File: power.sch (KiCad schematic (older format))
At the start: 13 parts, among them P1 POWER, Q2 DMP3056L-7, U1 REG1117-3.3, U2 REG1117A-2.5, U3 REG1117A-1.8

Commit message: Assigned footprints to most components
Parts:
- removed C9: 1uF, symbol CP1
- added C9: 1uF, Capacitors_SMD:C_0805, symbol C
- C10, C11, C12, C13, C14, C15: footprint (none) -> Capacitors_Tantalum_SMD:CP_Tantalum_Case-C_EIA-6032-28_Reflow
- F1: footprint (none) -> Fuse_Holders_and_Fuses:Fuse_CB61F
- P1: footprint (none) -> Connectors:USB_Micro-B
- Q2: footprint (none) -> TO_SOT_Packages_SMD:SOT-23
- U1, U2, U3: footprint SOT-223 -> TO_SOT_Packages_SMD:SOT-223-3_TabPin2
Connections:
- net +5V: now also C9.1
- net GND: now also C9.2
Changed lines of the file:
@@
 F 0 "U1" H 4000 1750 50  0000 C CNN
 F 1 "REG1117-3.3" H 4000 1700 50  0000 C CNN
-F 2 "SOT-223" H 4000 1600 50  0000 C CNN
+F 2 "TO_SOT_Packages_SMD:SOT-223-3_TabPin2" H 4000 1600 50  0000 C CNN
 F 3 "" H 4000 1500 50  0000 C CNN
 	1    4000 1500
@@
 F 0 "U2" H 6100 1750 50  0000 C CNN
 F 1 "REG1117A-2.5" H 6100 1700 50  0000 C CNN
-F 2 "SOT-223" H 6100 1600 50  0000 C CNN
+F 2 "TO_SOT_Packages_SMD:SOT-223-3_TabPin2" H 6100 1600 50  0000 C CNN
 F 3 "" H 6100 1500 50  0000 C CNN
 	1    6100 1500
@@
 F 0 "U3" H 8100 1750 50  0000 C CNN
 F 1 "REG1117A-1.8" H 8100 1700 50  0000 C CNN
-F 2 "SOT-223" H 8100 1600 50  0000 C CNN
+F 2 "TO_SOT_Packages_SMD:SOT-223-3_TabPin2" H 8100 1600 50  0000 C CNN
 F 3 "" H 8100 1500 50  0000 C CNN
 	1    8100 1500
@@
 F 0 "C10" H 3325 1900 50  0000 L CNN
 F 1 "10uF" H 3325 1700 50  0000 L CNN
-F 2 "" H 3300 1800 50  0000 C CNN
+F 2 "Capacitors_Tantalum_SMD:CP_Tantalum_Case-C_EIA-6032-28_Reflow" H 3300 1800 50  0001 C CNN
 F 3 "" H 3300 1800 50  0000 C CNN
 	1    3300 1800
@@
 F 0 "C12" H 5425 1900 50  0000 L CNN
 F 1 "10uF" H 5425 1700 50  0000 L CNN
-F 2 "" H 5400 1800 50  0000 C CNN
+F 2 "Capacitors_Tantalum_SMD:CP_Tantalum_Case-C_EIA-6032-28_Reflow" H 5400 1800 50  0001 C CNN
 F 3 "" H 5400 1800 50  0000 C CNN
 	1    5400 1800
@@
 F 0 "C11" H 4725 1900 50  0000 L CNN
 F 1 "10uF" H 4725 1700 50  0000 L CNN
-F 2 "" H 4700 1800 50  0000 C CNN
+F 2 "Capacitors_Tantalum_SMD:CP_Tantalum_Case-C_EIA-6032-28_Reflow" H 4700 1800 50  0001 C CNN
 F 3 "" H 4700 1800 50  0000 C CNN
 	1    4700 1800
@@
 F 0 "C13" H 6825 1900 50  0000 L CNN
 F 1 "10uF" H 6825 1700 50  0000 L CNN
-F 2 "" H 6800 1800 50  0000 C CNN
+F 2 "Capacitors_Tantalum_SMD:CP_Tantalum_Case-C_EIA-6032-28_Reflow" H 6800 1800 50  0001 C CNN
 F 3 "" H 6800 1800 50  0000 C CNN
 	1    6800 1800
@@
 F 0 "C14" H 7425 1900 50  0000 L CNN
 F 1 "10uF" H 7425 1700 50  0000 L CNN
-F 2 "" H 7400 1800 50  0000 C CNN
+F 2 "Capacitors_Tantalum_SMD:CP_Tantalum_Case-C_EIA-6032-28_Reflow" H 7400 1800 50  0001 C CNN
 F 3 "" H 7400 1800 50  0000 C CNN
 	1    7400 1800
@@
 F 0 "C15" H 8825 1900 50  0000 L CNN
 F 1 "10uF" H 8825 1700 50  0000 L CNN
-F 2 "" H 8800 1800 50  0000 C CNN
+F 2 "Capacitors_Tantalum_SMD:CP_Tantalum_Case-C_EIA-6032-28_Reflow" H 8800 1800 50  0001 C CNN
 F 3 "" H 8800 1800 50  0000 C CNN
 	1    8800 1800
@@
 F 0 "P1" H 1475 1425 50  0000 C CNN
 F 1 "POWER" H 1150 1750 50  0000 C CNN
-F 2 "" V 1100 1450 50  0000 C CNN
+F 2 "Connectors:USB_Micro-B" V 1100 1450 50  0001 C CNN
 F 3 "" V 1100 1450 50  0000 C CNN
 	1    1150 1550
@@
 F 0 "F1" V 1780 1350 50  0000 C CNN
 F 1 "2.5A" V 1625 1350 50  0000 C CNN
-F 2 "" V 1630 1350 50  0000 C CNN
+F 2 "Fuse_Holders_and_Fuses:Fuse_CB61F" V 1630 1350 50  0001 C CNN
 F 3 "" H 1700 1350 50  0000 C CNN
 	1    1700 1350
 	0    1    1    0
-$EndComp
-$Comp
-L CP1 C9
-U 1 1 5C122ABE
-P 2600 1800
-F 0 "C9" H 2625 1900 50  0000 L CNN
-F 1 "1uF" H 2625 1700 50  0000 L CNN
-F 2 "" H 2600 1800 50  0000 C CNN
-F 3 "" H 2600 1800 50  0000 C CNN
-	1    2600 1800
-	1    0    0    -1
 $EndComp
 $Comp
@@
 F 0 "Q2" H 2350 1500 50  0000 L CNN
 F 1 "DMP3056L-7" H 2350 1400 50  0000 L CNN
-F 2 "" H 2350 1550 50  0000 C CNN
+F 2 "TO_SOT_Packages_SMD:SOT-23" H 2350 1550 50  0001 C CNN
 F 3 "" H 2150 1450 50  0000 C CNN
 	1    2150 1450
@@
 Wire Wire Line
 	9450 2100 9450 1000
+$Comp
+L C C9
+U 1 1 5C14646A
+P 2600 1800
+F 0 "C9" H 2625 1900 50  0000 L CNN
+F 1 "1uF" H 2625 1700 50  0000 L CNN
+F 2 "Capacitors_SMD:C_0805" H 2638 1650 50  0001 C CNN
+F 3 "" H 2600 1800 50  0000 C CNN
+	1    2600 1800
+	1    0    0    -1
+$EndComp
 $EndSCHEMATC

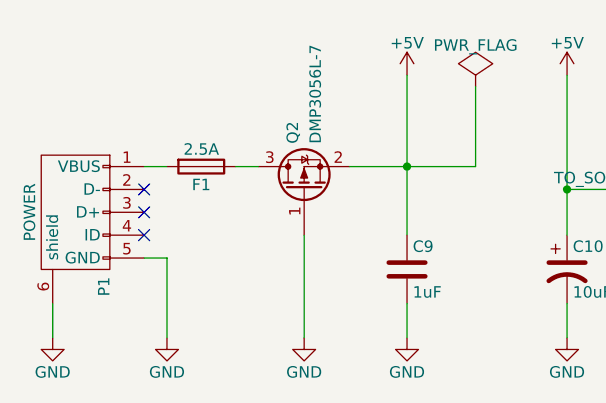
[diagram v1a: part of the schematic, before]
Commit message: Fixed fused
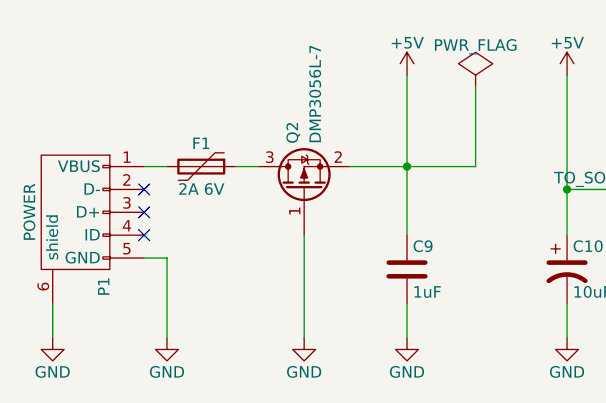
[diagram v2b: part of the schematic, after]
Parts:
- removed F1: 2.5A, Fuse_Holders_and_Fuses:Fuse_CB61F, symbol Fuse
- added F1: 2A 6V, Polyfuse_Bourns_MF-PSML:Polyfuse_0805, symbol Polyfuse
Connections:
- net at P1.1 (VBUS): now also F1.2
- net at Q2.3 (D): now also F1.1
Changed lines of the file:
@@
-$EndComp
-$Comp
-L Fuse F1
-U 1 1 5C1225FC
-P 1700 1350
-F 0 "F1" V 1780 1350 50  0000 C CNN
-F 1 "2.5A" V 1625 1350 50  0000 C CNN
-F 2 "Fuse_Holders_and_Fuses:Fuse_CB61F" V 1630 1350 50  0001 C CNN
-F 3 "" H 1700 1350 50  0000 C CNN
-	1    1700 1350
-	0    1    1    0
 $EndComp
 $Comp
@@
 	1    0    0    -1
 $EndComp
+$Comp
+L Polyfuse F1
+U 1 1 5C16EB7F
+P 1700 1350
+F 0 "F1" V 1600 1350 50  0000 C CNN
+F 1 "2A 6V" V 1800 1350 50  0000 C CNN
+F 2 "Polyfuse_Bourns_MF-PSML:Polyfuse_0805" H 1750 1150 50  0001 L CNN
+F 3 "" H 1700 1350 50  0001 C CNN
+	1    1700 1350
+	0    1    1    0
+$EndComp
 $EndSCHEMATC

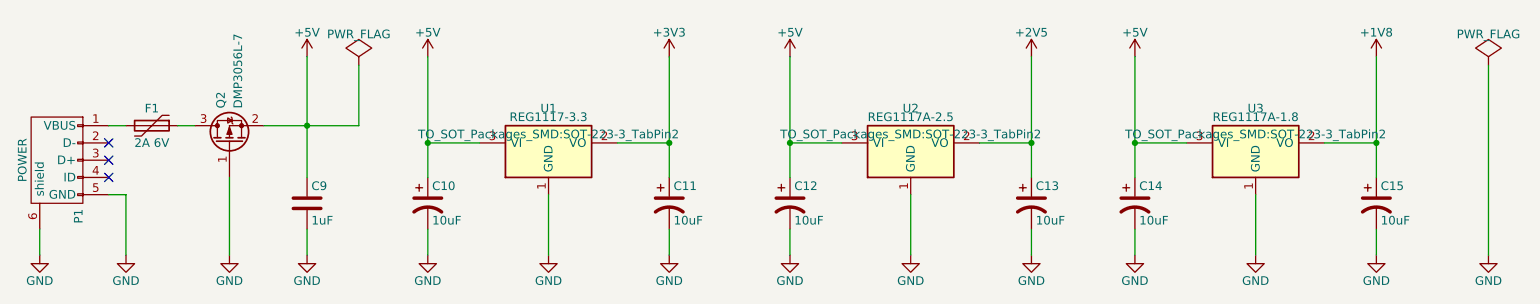
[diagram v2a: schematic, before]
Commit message: Removed 2.5V regulator and changed bottom ground plane clearence
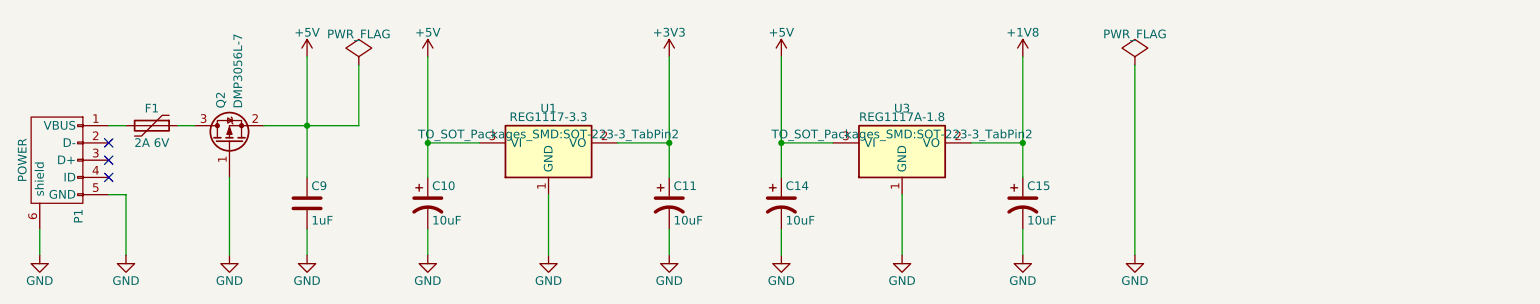
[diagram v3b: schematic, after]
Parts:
- removed C12, C13: 10uF, Capacitors_Tantalum_SMD:CP_Tantalum_Case-C_EIA-6032-28_Reflow, symbol CP1
- removed U2: REG1117A-2.5, TO_SOT_Packages_SMD:SOT-223-3_TabPin2, symbol REG1117A-2.5
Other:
- moved on the sheet: C14, C15, U3
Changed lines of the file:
@@
-$EndComp
-$Comp
-L REG1117A-2.5 U2
-U 1 1 5C11A1F2
-P 6100 1500
-F 0 "U2" H 6100 1750 50  0000 C CNN
-F 1 "REG1117A-2.5" H 6100 1700 50  0000 C CNN
-F 2 "TO_SOT_Packages_SMD:SOT-223-3_TabPin2" H 6100 1600 50  0000 C CNN
-F 3 "" H 6100 1500 50  0000 C CNN
-	1    6100 1500
-	1    0    0    -1
 $EndComp
 $Comp
 L REG1117A-1.8 U3
 U 1 1 5C11A22F
-P 8100 1500
-F 0 "U3" H 8100 1750 50  0000 C CNN
-F 1 "REG1117A-1.8" H 8100 1700 50  0000 C CNN
-F 2 "TO_SOT_Packages_SMD:SOT-223-3_TabPin2" H 8100 1600 50  0000 C CNN
-F 3 "" H 8100 1500 50  0000 C CNN
-	1    8100 1500
+P 6050 1500
+F 0 "U3" H 6050 1750 50  0000 C CNN
+F 1 "REG1117A-1.8" H 6050 1700 50  0000 C CNN
+F 2 "TO_SOT_Packages_SMD:SOT-223-3_TabPin2" H 6050 1600 50  0000 C CNN
+F 3 "" H 6050 1500 50  0000 C CNN
+	1    6050 1500
 	1    0    0    -1
 $EndComp
@@
 $EndComp
 $Comp
-L +5V #PWR031
-U 1 1 5C11A6C8
-P 5400 950
-F 0 "#PWR031" H 5400 800 50  0001 C CNN
-F 1 "+5V" H 5400 1090 50  0000 C CNN
-F 2 "" H 5400 950 50  0000 C CNN
-F 3 "" H 5400 950 50  0000 C CNN
-	1    5400 950
-	1    0    0    -1
-$EndComp
-$Comp
-L CP1 C12
-U 1 1 5C11A6CF
-P 5400 1800
-F 0 "C12" H 5425 1900 50  0000 L CNN
-F 1 "10uF" H 5425 1700 50  0000 L CNN
-F 2 "Capacitors_Tantalum_SMD:CP_Tantalum_Case-C_EIA-6032-28_Reflow" H 5400 1800 50  0001 C CNN
-F 3 "" H 5400 1800 50  0000 C CNN
-	1    5400 1800
-	1    0    0    -1
-$EndComp
-$Comp
-L GND #PWR032
-U 1 1 5C11A6D7
-P 5400 2100
-F 0 "#PWR032" H 5400 1850 50  0001 C CNN
-F 1 "GND" H 5400 1950 50  0000 C CNN
-F 2 "" H 5400 2100 50  0000 C CNN
-F 3 "" H 5400 2100 50  0000 C CNN
-	1    5400 2100
-	1    0    0    -1
-$EndComp
-$Comp
-L GND #PWR033
-U 1 1 5C11A6DD
-P 6100 2100
-F 0 "#PWR033" H 6100 1850 50  0001 C CNN
-F 1 "GND" H 6100 1950 50  0000 C CNN
-F 2 "" H 6100 2100 50  0000 C CNN
-F 3 "" H 6100 2100 50  0000 C CNN
-	1    6100 2100
-	1    0    0    -1
-$EndComp
-$Comp
 L CP1 C11
 U 1 1 5C11A780
@@
 $EndComp
 $Comp
-L CP1 C13
-U 1 1 5C11A7E8
-P 6800 1800
-F 0 "C13" H 6825 1900 50  0000 L CNN
-F 1 "10uF" H 6825 1700 50  0000 L CNN
-F 2 "Capacitors_Tantalum_SMD:CP_Tantalum_Case-C_EIA-6032-28_Reflow" H 6800 1800 50  0001 C CNN
-F 3 "" H 6800 1800 50  0000 C CNN
-	1    6800 1800
-	1    0    0    -1
-$EndComp
-$Comp
-L GND #PWR035
-U 1 1 5C11A7EF
-P 6800 2100
-F 0 "#PWR035" H 6800 1850 50  0001 C CNN
-F 1 "GND" H 6800 1950 50  0000 C CNN
-F 2 "" H 6800 2100 50  0000 C CNN
-F 3 "" H 6800 2100 50  0000 C CNN
-	1    6800 2100
-	1    0    0    -1
-$EndComp
-$Comp
 L +5V #PWR036
 U 1 1 5C11A92B
-P 7400 950
-F 0 "#PWR036" H 7400 800 50  0001 C CNN
-F 1 "+5V" H 7400 1090 50  0000 C CNN
-F 2 "" H 7400 950 50  0000 C CNN
-F 3 "" H 7400 950 50  0000 C CNN
-	1    7400 950
+P 5350 950
+F 0 "#PWR036" H 5350 800 50  0001 C CNN
+F 1 "+5V" H 5350 1090 50  0000 C CNN
+F 2 "" H 5350 950 50  0000 C CNN
+F 3 "" H 5350 950 50  0000 C CNN
+	1    5350 950
 	1    0    0    -1
 $EndComp
@@
 L CP1 C14
 U 1 1 5C11A932
-P 7400 1800
-F 0 "C14" H 7425 1900 50  0000 L CNN
-F 1 "10uF" H 7425 1700 50  0000 L CNN
-F 2 "Capacitors_Tantalum_SMD:CP_Tantalum_Case-C_EIA-6032-28_Reflow" H 7400 1800 50  0001 C CNN
-F 3 "" H 7400 1800 50  0000 C CNN
-	1    7400 1800
+P 5350 1800
+F 0 "C14" H 5375 1900 50  0000 L CNN
+F 1 "10uF" H 5375 1700 50  0000 L CNN
+F 2 "Capacitors_Tantalum_SMD:CP_Tantalum_Case-C_EIA-6032-28_Reflow" H 5350 1800 50  0001 C CNN
+F 3 "" H 5350 1800 50  0000 C CNN
+	1    5350 1800
 	1    0    0    -1
 $EndComp
@@
 L GND #PWR037
 U 1 1 5C11A93A
-P 7400 2100
-F 0 "#PWR037" H 7400 1850 50  0001 C CNN
-F 1 "GND" H 7400 1950 50  0000 C CNN
-F 2 "" H 7400 2100 50  0000 C CNN
-F 3 "" H 7400 2100 50  0000 C CNN
-	1    7400 2100
+P 5350 2100
+F 0 "#PWR037" H 5350 1850 50  0001 C CNN
+F 1 "GND" H 5350 1950 50  0000 C CNN
+F 2 "" H 5350 2100 50  0000 C CNN
+F 3 "" H 5350 2100 50  0000 C CNN
+	1    5350 2100
 	1    0    0    -1
 $EndComp
@@
 L GND #PWR038
 U 1 1 5C11A940
-P 8100 2100
-F 0 "#PWR038" H 8100 1850 50  0001 C CNN
-F 1 "GND" H 8100 1950 50  0000 C CNN
-F 2 "" H 8100 2100 50  0000 C CNN
-F 3 "" H 8100 2100 50  0000 C CNN
-	1    8100 2100
+P 6050 2100
+F 0 "#PWR038" H 6050 1850 50  0001 C CNN
+F 1 "GND" H 6050 1950 50  0000 C CNN
+F 2 "" H 6050 2100 50  0000 C CNN
+F 3 "" H 6050 2100 50  0000 C CNN
+	1    6050 2100
 	1    0    0    -1
 $EndComp
@@
 L CP1 C15
 U 1 1 5C11A94D
-P 8800 1800
-F 0 "C15" H 8825 1900 50  0000 L CNN
-F 1 "10uF" H 8825 1700 50  0000 L CNN
-F 2 "Capacitors_Tantalum_SMD:CP_Tantalum_Case-C_EIA-6032-28_Reflow" H 8800 1800 50  0001 C CNN
-F 3 "" H 8800 1800 50  0000 C CNN
-	1    8800 1800
+P 6750 1800
+F 0 "C15" H 6775 1900 50  0000 L CNN
+F 1 "10uF" H 6775 1700 50  0000 L CNN
+F 2 "Capacitors_Tantalum_SMD:CP_Tantalum_Case-C_EIA-6032-28_Reflow" H 6750 1800 50  0001 C CNN
+F 3 "" H 6750 1800 50  0000 C CNN
+	1    6750 1800
 	1    0    0    -1
 $EndComp
@@
 L GND #PWR039
 U 1 1 5C11A954
-P 8800 2100
-F 0 "#PWR039" H 8800 1850 50  0001 C CNN
-F 1 "GND" H 8800 1950 50  0000 C CNN
-F 2 "" H 8800 2100 50  0000 C CNN
-F 3 "" H 8800 2100 50  0000 C CNN
-	1    8800 2100
-	1    0    0    -1
-$EndComp
-$Comp
-L +2V5 #PWR040
-U 1 1 5C11AE1D
-P 6800 950
-F 0 "#PWR040" H 6800 800 50  0001 C CNN
-F 1 "+2V5" H 6800 1090 50  0000 C CNN
-F 2 "" H 6800 950 50  0000 C CNN
-F 3 "" H 6800 950 50  0000 C CNN
-	1    6800 950
+P 6750 2100
+F 0 "#PWR039" H 6750 1850 50  0001 C CNN
+F 1 "GND" H 6750 1950 50  0000 C CNN
+F 2 "" H 6750 2100 50  0000 C CNN
+F 3 "" H 6750 2100 50  0000 C CNN
+	1    6750 2100
 	1    0    0    -1
 $EndComp
@@
 L +1V8 #PWR041
 U 1 1 5C11AE43
-P 8800 950
-F 0 "#PWR041" H 8800 800 50  0001 C CNN
-F 1 "+1V8" H 8800 1090 50  0000 C CNN
-F 2 "" H 8800 950 50  0000 C CNN
-F 3 "" H 8800 950 50  0000 C CNN
-	1    8800 950
+P 6750 950
+F 0 "#PWR041" H 6750 800 50  0001 C CNN
+F 1 "+1V8" H 6750 1090 50  0000 C CNN
+F 2 "" H 6750 950 50  0000 C CNN
+F 3 "" H 6750 950 50  0000 C CNN
+	1    6750 950
 	1    0    0    -1
 $EndComp
@@
 	3300 1950 3300 2100
 Wire Wire Line
-	5700 1450 5400 1450
-Wire Wire Line
-	5400 950  5400 1650
-Wire Wire Line
-	6500 1450 6800 1450
-Wire Wire Line
-	6800 950  6800 1650
-Wire Wire Line
-	6100 1750 6100 2100
-Connection ~ 5400 1450
-Wire Wire Line
-	5400 1950 5400 2100
-Wire Wire Line
 	4700 1950 4700 2100
 Wire Wire Line
-	6800 1950 6800 2100
-Wire Wire Line
-	7700 1450 7400 1450
-Wire Wire Line
-	7400 950  7400 1650
-Wire Wire Line
-	8500 1450 8800 1450
-Wire Wire Line
-	8800 950  8800 1650
-Wire Wire Line
-	8100 1750 8100 2100
-Connection ~ 7400 1450
-Wire Wire Line
-	7400 1950 7400 2100
-Wire Wire Line
-	8800 1950 8800 2100
+	5650 1450 5350 1450
+Wire Wire Line
+	5350 950  5350 1650
+Wire Wire Line
+	6450 1450 6750 1450
+Wire Wire Line
+	6750 950  6750 1650
+Wire Wire Line
+	6050 1750 6050 2100
+Connection ~ 5350 1450
+Wire Wire Line
+	5350 1950 5350 2100
+Wire Wire Line
+	6750 1950 6750 2100
 Wire Wire Line
 	1050 2100 1050 1950
@@
 Connection ~ 2600 1350
 Connection ~ 4700 1450
-Connection ~ 8800 1450
-Connection ~ 6800 1450
+Connection ~ 6750 1450
 $Comp
 L PWR_FLAG #FLG047
@@
 L PWR_FLAG #FLG048
 U 1 1 5C13F5FD
-P 9450 1000
-F 0 "#FLG048" H 9450 1095 50  0001 C CNN
-F 1 "PWR_FLAG" H 9450 1180 50  0000 C CNN
-F 2 "" H 9450 1000 50  0000 C CNN
-F 3 "" H 9450 1000 50  0000 C CNN
-	1    9450 1000
+P 7400 1000
+F 0 "#FLG048" H 7400 1095 50  0001 C CNN
+F 1 "PWR_FLAG" H 7400 1180 50  0000 C CNN
+F 2 "" H 7400 1000 50  0000 C CNN
+F 3 "" H 7400 1000 50  0000 C CNN
+	1    7400 1000
 	1    0    0    -1
 $EndComp
@@
 L GND #PWR049
 U 1 1 5C13F62F
-P 9450 2100
-F 0 "#PWR049" H 9450 1850 50  0001 C CNN
-F 1 "GND" H 9450 1950 50  0000 C CNN
-F 2 "" H 9450 2100 50  0000 C CNN
-F 3 "" H 9450 2100 50  0000 C CNN
-	1    9450 2100
-	1    0    0    -1
-$EndComp
-Wire Wire Line
-	9450 2100 9450 1000
+P 7400 2100
+F 0 "#PWR049" H 7400 1850 50  0001 C CNN
+F 1 "GND" H 7400 1950 50  0000 C CNN
+F 2 "" H 7400 2100 50  0000 C CNN
+F 3 "" H 7400 2100 50  0000 C CNN
+	1    7400 2100
+	1    0    0    -1
+$EndComp
+Wire Wire Line
+	7400 2100 7400 1000
 $Comp
 L C C9

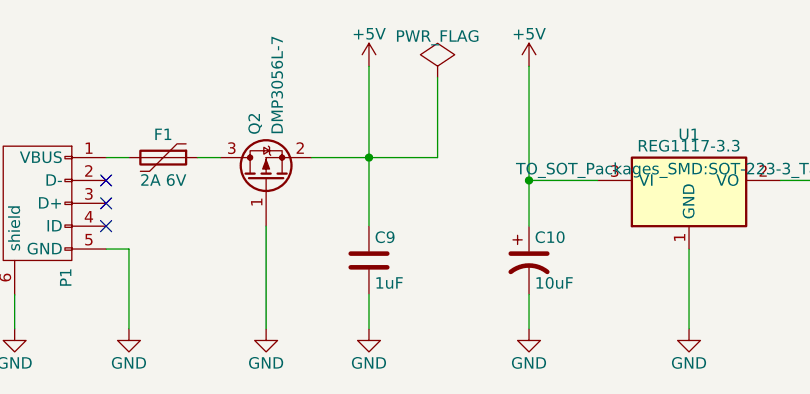
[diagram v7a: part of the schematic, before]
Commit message: Replaced 1uF input cap with 100nF
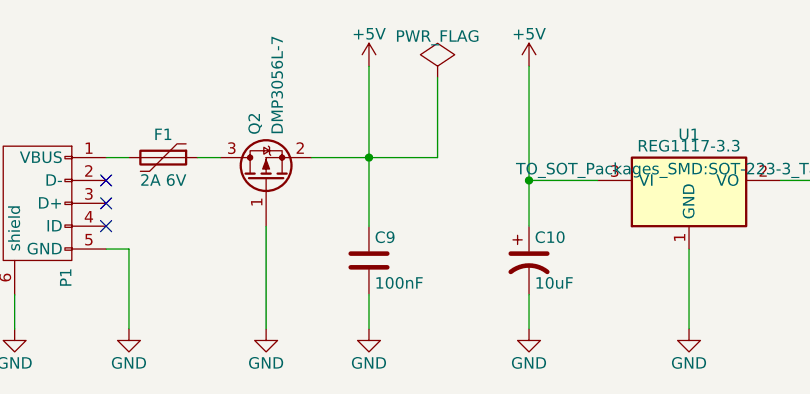
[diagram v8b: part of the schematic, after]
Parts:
- C9: value 1uF -> 100nF; footprint Capacitors_SMD:C_0805 -> Capacitors_SMD:C_0402
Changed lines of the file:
@@
 P 2600 1800
 F 0 "C9" H 2625 1900 50  0000 L CNN
-F 1 "1uF" H 2625 1700 50  0000 L CNN
-F 2 "Capacitors_SMD:C_0805" H 2638 1650 50  0001 C CNN
+F 1 "100nF" H 2625 1700 50  0000 L CNN
+F 2 "Capacitors_SMD:C_0402" H 2638 1650 50  0001 C CNN
 F 3 "" H 2600 1800 50  0000 C CNN
 	1    2600 1800
